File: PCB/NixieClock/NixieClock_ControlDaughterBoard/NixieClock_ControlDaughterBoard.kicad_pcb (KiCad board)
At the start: 2 copper layers, 85.5 x 52 mm, 33 parts, among them J1 Conn_01x05, J3 Conn_01x04_Pin, J4 Conn_01x04_Pin, Q1 IRLML6244, Q2 IRLML6244, Q3 IRLML6402

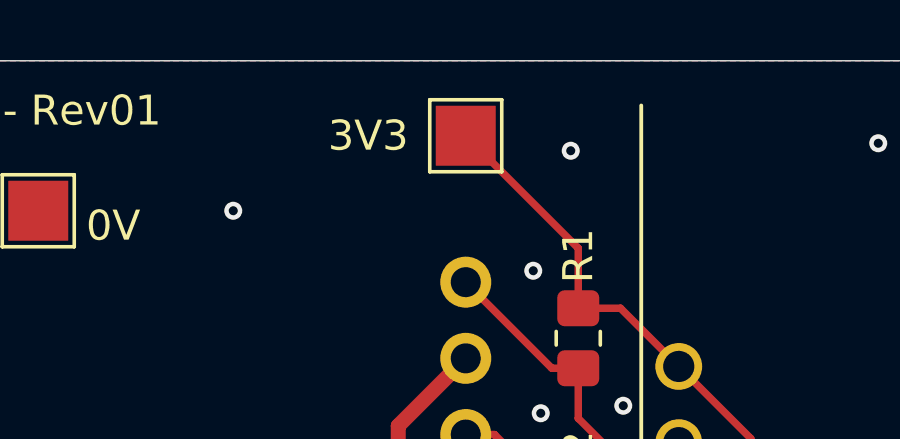
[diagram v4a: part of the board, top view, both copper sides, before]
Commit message: Add 2025 to silkscreen
add current year to project silkscreen. regenerate gerbers to suit
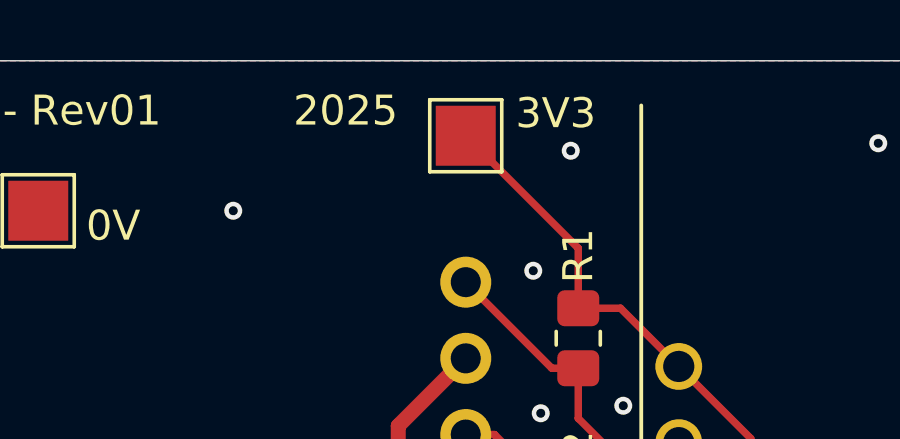
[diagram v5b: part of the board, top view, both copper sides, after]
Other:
- board text added: "2025"
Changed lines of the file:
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@@
 		)
 		(property "Value" "3V3"
-			(at -3.25 0 0)
+			(at 3 -0.75 0)
 			(layer "F.SilkS")
 			(effects
@@
 		(layer "F.SilkS")
 		(effects
+			(font
+				(size 1 1)
+				(thickness 0.15)
+			)
+			(justify left bottom)
+		)
+	)
+	(gr_text "2025"
+		(at 142.75 82.25 0)
+		(layer "F.SilkS")
+		(effects

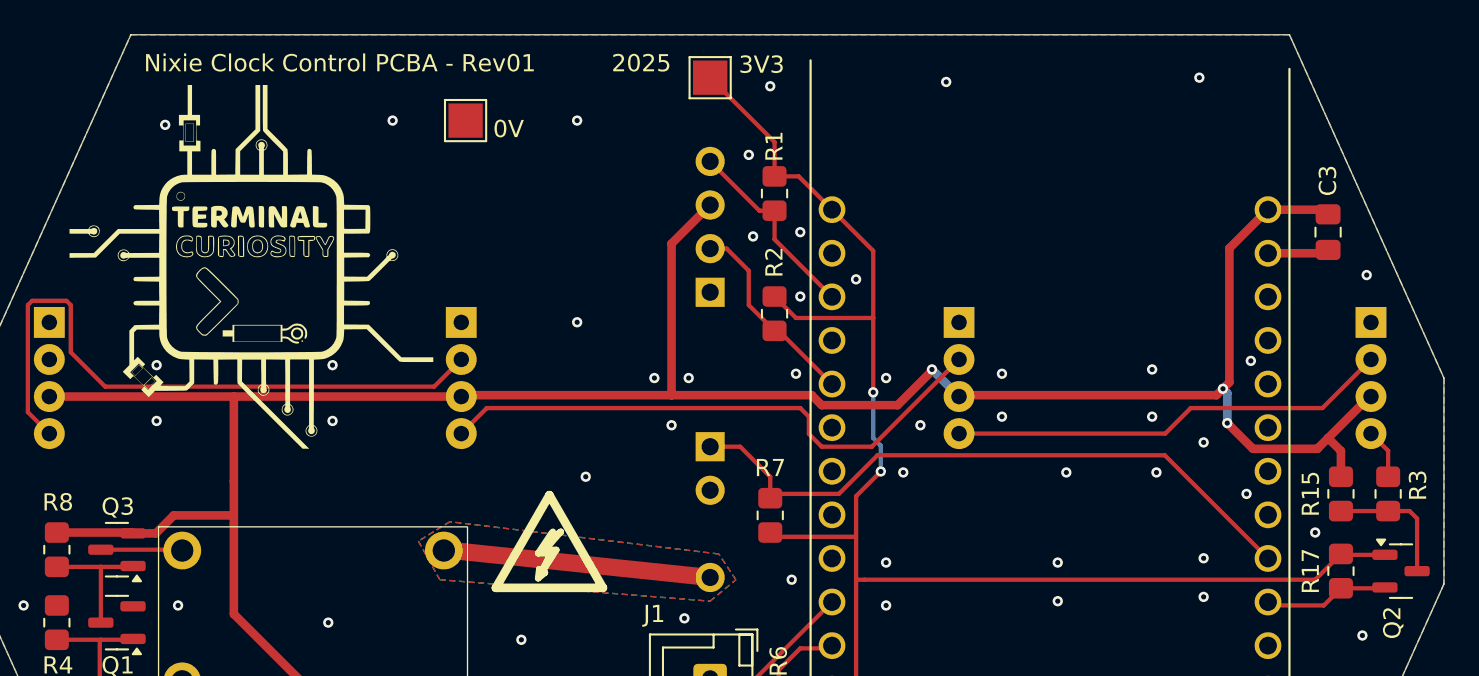
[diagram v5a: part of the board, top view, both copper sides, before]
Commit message: swap pins 1,2 on LEDs
LED pin layout was mistakenly swapped. discovered on Rev01 prototype. swapped pins in the SCH and PCB files. updated assembly to Rev02
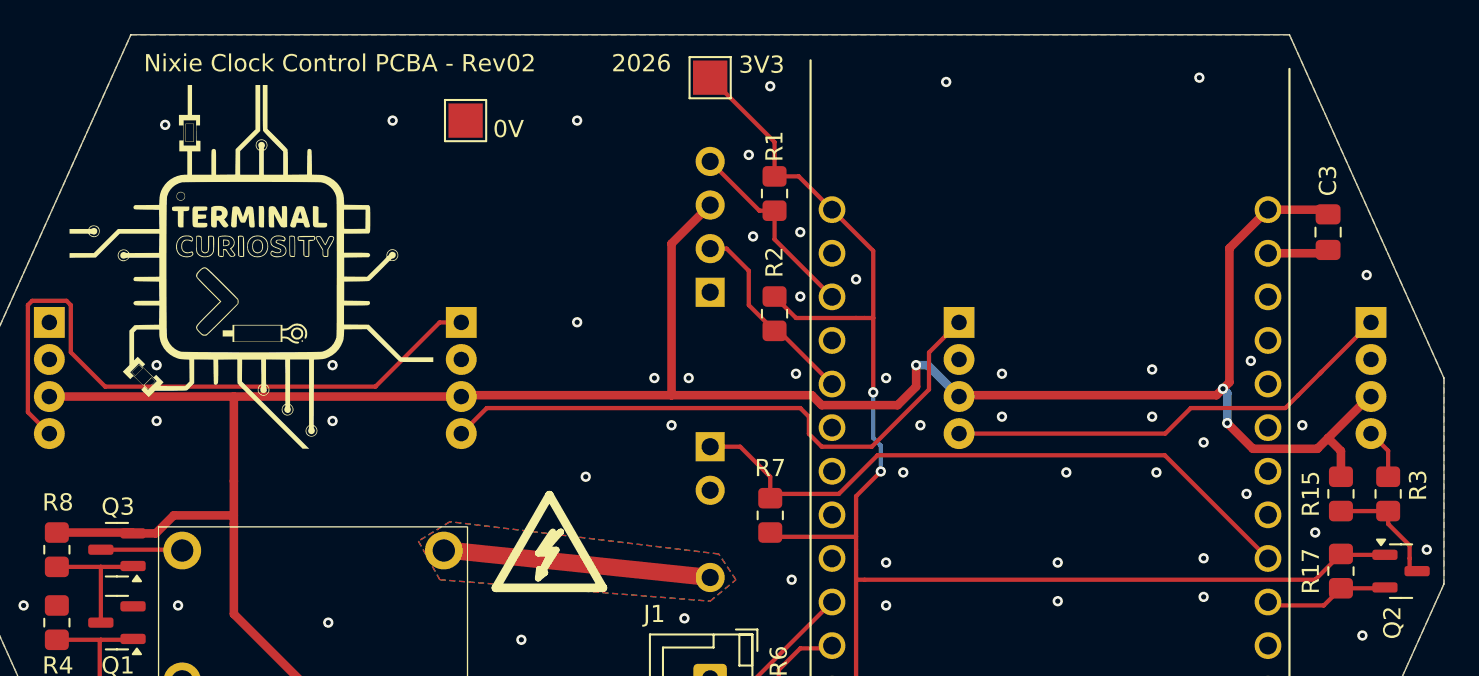
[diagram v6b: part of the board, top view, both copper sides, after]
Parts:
- J3, J4: value Conn_01x04_Pin -> Conn_01x04
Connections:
- D1 pad 1: GND -> Net-(D1-DOUT)
- D1 pad 2: Net-(D1-DOUT) -> GND
- D2 pad 1: GND -> Net-(D2-DOUT)
- D2 pad 2: Net-(D2-DOUT) -> GND
- D3 pad 1: GND -> Net-(D3-DOUT)
- D3 pad 2: Net-(D3-DOUT) -> GND
- D4 pad 1: GND -> unconnected-(D4-DOUT-Pad1)
- D4 pad 2: unconnected-(D4-DOUT-Pad2) -> GND
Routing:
- net Net-(D2-DOUT): track 33.2 -> 35.4 mm
- net Net-(D1-DOUT): track 25.8 -> 26.9 mm
- net /LED-Data_5V: track 7.68 -> 6.77 mm
- net Net-(D3-DOUT): track 37.7 -> 38.6 mm
- net +5V: track 174.1 -> 175.0 mm
- net GND: vias 61 -> 63
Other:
- board text added: "2026"
- board text added: "Nixie Clock Control PCBA - Rev02"
- board text removed: "2025"
- board text removed: "Nixie Clock Control PCBA - Rev01"
